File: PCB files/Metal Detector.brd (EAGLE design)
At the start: 100 x 80 mm, 61 parts, among them IC1 NE5534AD, IC2 BQ24133RGYR, IC3 MC33269D-5.0G, IC4 ESP32-WROOM-32UE-N4, IC5 CP2102, IC6 NCP1117DT12G, Q1 IRF740, Q2 BC556, Q4 MBT3904DW1T1, T1 BC547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

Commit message: Add files via upload
Design process still on progress
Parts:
- added C6: 1uF/16v, rcl:C0603
- added R13: 10R, rcl:R1206
- added R15: 2R2, rcl:R2010
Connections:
- removed net 1: X2.1
- removed net 2: X2.2
- removed net 3: X2.3
- new net EXT_PWR_IN: IC3.4, IC6.3, X2.2
- new net N$14: C6.2, IC2.4, R13.2
- net GND: now also IC3.1, IC6.1, X2.1, X2.3
- net VCC: now also IC6.2
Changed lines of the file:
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@@
 <attribute name="VALUE" x="-114.34" y="-165.1" size="1.27" layer="27" align="center"/>
+</element>
+<element name="C6" library="rcl" library_urn="urn:adsk.eagle:library:334" package="C0603" package3d_urn="urn:adsk.eagle:package:23616/2" value="1uF/16v" x="-120.65" y="-175.26" smashed="yes">
+<attribute name="NAME" x="-121.285" y="-174.625" size="1.27" layer="25"/>
+<attribute name="POPULARITY" value="73" x="-120.65" y="-175.26" size="1.778" layer="27" display="off"/>
+<attribute name="SPICEPREFIX" value="C" x="-120.65" y="-175.26" size="1.778" layer="27" display="off"/>
+<attribute name="VALUE" x="-121.285" y="-177.165" size="1.27" layer="27"/>
+</element>
+<element name="R15" library="rcl" library_urn="urn:adsk.eagle:library:334" package="R2010" package3d_urn="urn:adsk.eagle:package:23551/2" value="2R2" x="-119.38" y="-232.41" smashed="yes">
+<attribute name="NAME" x="-122.555" y="-230.505" size="1.27" layer="25"/>
+<attribute name="POPULARITY" value="3" x="-119.38" y="-232.41" size="1.778" layer="27" display="off"/>
+<attribute name="SPICEPREFIX" value="R" x="-119.38" y="-232.41" size="1.778" layer="27" display="off"/>
+<attribute name="VALUE" x="-122.555" y="-235.585" size="1.27" layer="27"/>
+</element>
+<element name="R13" library="rcl" library_urn="urn:adsk.eagle:library:334" package="R1206" package3d_urn="urn:adsk.eagle:package:23540/2" value="10R" x="-120.65" y="-240.03" smashed="yes">
+<attribute name="NAME" x="-121.92" y="-238.76" size="1.27" layer="25"/>
+<attribute name="POPULARITY" value="41" x="-120.65" y="-240.03" size="1.778" layer="27" display="off"/>
+<attribute name="SPICEPREFIX" value="R" x="-120.65" y="-240.03" size="1.778" layer="27" display="off"/>
+<attribute name="VALUE" x="-121.92" y="-242.57" size="1.27" layer="27"/>
 </element>
 </elements>
@@
 <contactref element="D4" pad="2"/>
 <contactref element="D8" pad="2"/>
+<contactref element="X2" pad="1"/>
+<contactref element="X2" pad="3"/>
+<contactref element="IC6" pad="1"/>
+<contactref element="IC3" pad="1"/>
+<wire x1="-75.102" y1="-86.995" x2="-67.25" y2="-98.805" width="0" layer="19" extent="1-1"/>
+<wire x1="-73.66" y1="-79.5528" x2="-75.102" y2="-86.995" width="0" layer="19" extent="1-1"/>
+<wire x1="-68.6562" y1="-76.5556" x2="-73.66" y2="-79.5528" width="0" layer="19" extent="1-1"/>
+<wire x1="-68.255" y1="-59.69" x2="-68.6562" y2="-76.5556" width="0" layer="19" extent="1-1"/>
+<wire x1="-74.51" y1="-50.8" x2="-68.255" y2="-59.69" width="0" layer="19" extent="1-1"/>
 <wire x1="-72.81" y1="-45.72" x2="-74.51" y2="-50.8" width="0" layer="19" extent="1-1"/>
 <wire x1="-74.51" y1="-40.64" x2="-72.81" y2="-45.72" width="0" layer="19" extent="1-1"/>
@@
 <wire x1="-72.25" y1="-13.18" x2="-66.4" y2="-19.12" width="0" layer="19" extent="1-1"/>
 <wire x1="-54.75" y1="-13.18" x2="-63.6" y2="-19.12" width="0" layer="19" extent="1-1"/>
-<wire x1="-68.255" y1="-59.69" x2="-74.51" y2="-50.8" width="0" layer="19" extent="1-1"/>
 <wire x1="-44.265" y1="-19.08" x2="-54.75" y2="-13.18" width="0" layer="19" extent="1-1"/>
 <wire x1="-41.72" y1="-13.47" x2="-44.265" y2="-19.08" width="0" layer="19" extent="1-1"/>
@@
 <contactref element="R18" pad="2"/>
 <contactref element="F2" pad="2"/>
+<contactref element="IC6" pad="2"/>
+<wire x1="-64.64" y1="-55.88" x2="-74.43" y2="-96.52" width="0" layer="19" extent="1-1"/>
 <wire x1="-63.92" y1="-50.8" x2="-64.64" y2="-55.88" width="0" layer="19" extent="1-1"/>
 <wire x1="-58.84" y1="-50.8" x2="-63.92" y2="-50.8" width="0" layer="19" extent="1-1"/>
@@
 <wire x1="-39.87" y1="-11.62" x2="-40.22" y2="-50.8" width="0" layer="19" extent="1-1"/>
 </signal>
-<signal name="1">
-<contactref element="X2" pad="1"/>
-</signal>
-<signal name="2">
+<signal name="EXT_PWR_IN">
 <contactref element="X2" pad="2"/>
-</signal>
-<signal name="3">
-<contactref element="X2" pad="3"/>
+<contactref element="IC3" pad="4"/>
+<contactref element="IC6" pad="3"/>
+<wire x1="-67.25" y1="-94.235" x2="-75.102" y2="-90.805" width="0" layer="19" extent="1-1"/>
+<wire x1="-68.6562" y1="-82.55" x2="-75.102" y2="-90.805" width="0" layer="19" extent="1-1"/>
+</signal>
+<signal name="N$14">
+<contactref element="IC2" pad="4"/>
+<contactref element="C6" pad="2"/>
+<contactref element="R13" pad="2"/>
+<wire x1="-119.8" y1="-175.26" x2="-71.1" y2="-66.495" width="0" layer="19" extent="1-1"/>
+<wire x1="-119.228" y1="-240.03" x2="-119.8" y2="-175.26" width="0" layer="19" extent="1-1"/>
 </signal>
 </signals>

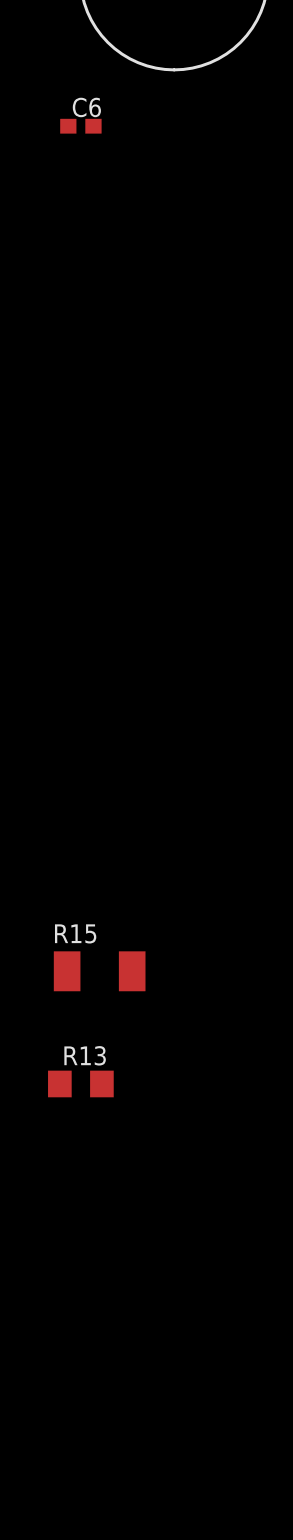
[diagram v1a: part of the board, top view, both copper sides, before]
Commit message: Add files via upload
Still designin power circuit but should be change battery charge IC for tehnical limitation
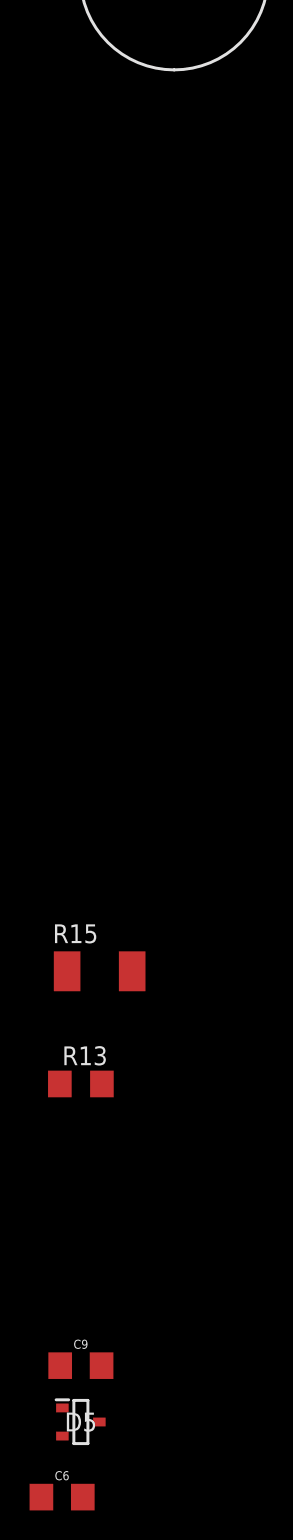
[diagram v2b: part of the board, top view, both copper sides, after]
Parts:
- added C9: 1.0uF/25 VDC/XR7, SparkFun-Capacitors:1206
- added D5: MMBD717, MMBD717:SOT95P240X110-3N
- C6: value 1uF/16v -> 2.2uF/25 VDC/XR7; device rcl:C0603 -> SparkFun-Capacitors:1206
- moved C6 92.7 mm to (-121.9, -268.0)
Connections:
- new net ACDRV: IC2.8
- new net ACN: IC2.5
- new net ACP: IC2.6
- new net ACSET: IC2.17
- new net AGND: IC2.25
- new net AVCC: C9.1, IC2.4, R13.2
- new net BATDRV: IC2.19
- new net BTST: IC2.21
- new net CELL: IC2.14
- new net CMSRC: IC2.7
- new net ISET: IC2.13
- new net N$16: C6.1, R15.1
- new net OVPSET: IC2.18
- new net PGND_1: IC2.22
- new net PGND_2: IC2.23
- new net PVCC_1: IC2.2
- new net PVCC_2: IC2.3
- new net REGN: IC2.20
- new net SRN: IC2.15
- new net SRP: IC2.16
- new net STAT: IC2.9
- new net SW_1: IC2.1
- new net SW_2: IC2.24
- new net TS: IC2.10
- new net TTC: IC2.11
- new net VBATT: D5.K2
- new net VREF: IC2.12
- net EXT_PWR_IN: now also D5.K1, R15.2
- net GND: now also C6.2, C9.2
- net N$14: now also D5.A, R13.1; no longer C6.2, IC2.4, R13.2
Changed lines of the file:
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@@
 <attribute name="VALUE" x="-114.34" y="-165.1" size="1.27" layer="27" align="center"/>
-</element>
-<element name="C6" library="rcl" library_urn="urn:adsk.eagle:library:334" package="C0603" package3d_urn="urn:adsk.eagle:package:23616/2" value="1uF/16v" x="-120.65" y="-175.26" smashed="yes">
-<attribute name="NAME" x="-121.285" y="-174.625" size="1.27" layer="25"/>
-<attribute name="POPULARITY" value="73" x="-120.65" y="-175.26" size="1.778" layer="27" display="off"/>
-<attribute name="SPICEPREFIX" value="C" x="-120.65" y="-175.26" size="1.778" layer="27" display="off"/>
-<attribute name="VALUE" x="-121.285" y="-177.165" size="1.27" layer="27"/>
 </element>
 <element name="R15" library="rcl" library_urn="urn:adsk.eagle:library:334" package="R2010" package3d_urn="urn:adsk.eagle:package:23551/2" value="2R2" x="-119.38" y="-232.41" smashed="yes">
@@
 <attribute name="SPICEPREFIX" value="R" x="-120.65" y="-240.03" size="1.778" layer="27" display="off"/>
 <attribute name="VALUE" x="-121.92" y="-242.57" size="1.27" layer="27"/>
+</element>
+<element name="C9" library="SparkFun-Capacitors" library_urn="urn:adsk.eagle:library:510" package="1206" package3d_urn="urn:adsk.eagle:package:41385095/1" value="1.0uF/25 VDC/XR7" x="-120.65" y="-259.08" smashed="yes">
+<attribute name="NAME" x="-120.65" y="-257.937" size="0.6096" layer="25" font="vector" ratio="20" align="bottom-center"/>
+<attribute name="PROD_ID" value="CAP-09822" x="-120.65" y="-259.08" size="1.778" layer="27" display="off"/>
+<attribute name="VALUE" x="-120.65" y="-260.223" size="0.6096" layer="27" font="vector" ratio="20" align="top-center"/>
+</element>
+<element name="D5" library="MMBD717" package="SOT95P240X110-3N" value="MMBD717" x="-120.65" y="-262.89" smashed="yes">
+<attribute name="ARROW_PART_NUMBER" value="" x="-120.65" y="-262.89" size="1.778" layer="27" display="off"/>
+<attribute name="ARROW_PRICE-STOCK" value="" x="-120.65" y="-262.89" size="1.778" layer="27" display="off"/>
+<attribute name="DESCRIPTION" value="Small Signal Schottky (IF&lt;1A) - MMBD717 , 20V, 1mA, SOT-23" x="-120.65" y="-262.89" size="1.778" layer="27" display="off"/>
+<attribute name="HEIGHT" value="1.1mm" x="-120.65" y="-262.89" size="1.778" layer="27" display="off"/>
+<attribute name="MANUFACTURER_NAME" value="PANJIT" x="-120.65" y="-262.89" size="1.778" layer="27" display="off"/>
+<attribute name="MANUFACTURER_PART_NUMBER" value="MMBD717" x="-120.65" y="-262.89" size="1.778" layer="27" display="off"/>
+<attribute name="MOUSER_PART_NUMBER" value="" x="-120.65" y="-262.89" size="1.778" layer="27" display="off"/>
+<attribute name="MOUSER_PRICE-STOCK" value="" x="-120.65" y="-262.89" size="1.778" layer="27" display="off"/>
+<attribute name="NAME" x="-120.65" y="-262.89" size="1.27" layer="25" align="center"/>
+<attribute name="VALUE" x="-120.65" y="-262.89" size="1.27" layer="27" align="center"/>
+</element>
+<element name="C6" library="SparkFun-Capacitors" library_urn="urn:adsk.eagle:library:510" package="1206" package3d_urn="urn:adsk.eagle:package:41385095/1" value="2.2uF/25 VDC/XR7" x="-121.92" y="-267.97" smashed="yes">
+<attribute name="NAME" x="-121.92" y="-266.827" size="0.6096" layer="25" font="vector" ratio="20" align="bottom-center"/>
+<attribute name="PROD_ID" value="CAP-09822" x="-121.92" y="-267.97" size="1.778" layer="27" display="off"/>
+<attribute name="VALUE" x="-121.92" y="-269.113" size="0.6096" layer="27" font="vector" ratio="20" align="top-center"/>
 </element>
 </elements>
@@
 <contactref element="IC6" pad="1"/>
 <contactref element="IC3" pad="1"/>
+<contactref element="C9" pad="2"/>
+<contactref element="C6" pad="2"/>
 <wire x1="-75.102" y1="-86.995" x2="-67.25" y2="-98.805" width="0" layer="19" extent="1-1"/>
 <wire x1="-73.66" y1="-79.5528" x2="-75.102" y2="-86.995" width="0" layer="19" extent="1-1"/>
@@
 <wire x1="-31.17" y1="77.47" x2="-34.98" y2="77.47" width="0" layer="19" extent="1-1"/>
 <wire x1="-26.67" y1="66.04" x2="-31.17" y2="77.47" width="0" layer="19" extent="1-1"/>
+<wire x1="-119.25" y1="-259.08" x2="-67.25" y2="-98.805" width="0" layer="19" extent="1-1"/>
+<wire x1="-120.52" y1="-267.97" x2="-119.25" y2="-259.08" width="0" layer="19" extent="1-1"/>
 </signal>
 <signal name="VCC">
@@
 <contactref element="IC3" pad="4"/>
 <contactref element="IC6" pad="3"/>
+<contactref element="R15" pad="2"/>
+<contactref element="D5" pad="K1"/>
 <wire x1="-67.25" y1="-94.235" x2="-75.102" y2="-90.805" width="0" layer="19" extent="1-1"/>
 <wire x1="-68.6562" y1="-82.55" x2="-75.102" y2="-90.805" width="0" layer="19" extent="1-1"/>
+<wire x1="-117.18" y1="-232.41" x2="-67.25" y2="-94.235" width="0" layer="19" extent="1-1"/>
+<wire x1="-121.9" y1="-261.94" x2="-117.18" y2="-232.41" width="0" layer="19" extent="1-1"/>
+</signal>
+<signal name="N$16">
+<contactref element="C6" pad="1"/>
+<contactref element="R15" pad="1"/>
+<wire x1="-121.58" y1="-232.41" x2="-123.32" y2="-267.97" width="0" layer="19" extent="1-1"/>
+</signal>
+<signal name="AVCC">
+<contactref element="IC2" pad="4"/>
+<contactref element="R13" pad="2"/>
+<contactref element="C9" pad="1"/>
+<wire x1="-119.228" y1="-240.03" x2="-71.1" y2="-66.495" width="0" layer="19" extent="1-1"/>
+<wire x1="-122.05" y1="-259.08" x2="-119.228" y2="-240.03" width="0" layer="19" extent="1-1"/>
+</signal>
+<signal name="VBATT">
+<contactref element="D5" pad="K2"/>
 </signal>
 <signal name="N$14">
-<contactref element="IC2" pad="4"/>
-<contactref element="C6" pad="2"/>
-<contactref element="R13" pad="2"/>
-<wire x1="-119.8" y1="-175.26" x2="-71.1" y2="-66.495" width="0" layer="19" extent="1-1"/>
-<wire x1="-119.228" y1="-240.03" x2="-119.8" y2="-175.26" width="0" layer="19" extent="1-1"/>
+<contactref element="D5" pad="A"/>
+<contactref element="R13" pad="1"/>
+<wire x1="-122.072" y1="-240.03" x2="-119.4" y2="-262.89" width="0" layer="19" extent="1-1"/>
+</signal>
+<signal name="PVCC_1">
+<contactref element="IC2" pad="2"/>
+</signal>
+<signal name="PVCC_2">
+<contactref element="IC2" pad="3"/>
+</signal>
+<signal name="ACN">
+<contactref element="IC2" pad="5"/>
+</signal>
+<signal name="ACP">
+<contactref element="IC2" pad="6"/>
+</signal>
+<signal name="CMSRC">
+<contactref element="IC2" pad="7"/>
+</signal>
+<signal name="ACDRV">
+<contactref element="IC2" pad="8"/>
+</signal>
+<signal name="STAT">
+<contactref element="IC2" pad="9"/>
+</signal>
+<signal name="TS">
+<contactref element="IC2" pad="10"/>
+</signal>
+<signal name="TTC">
+<contactref element="IC2" pad="11"/>
+</signal>
+<signal name="VREF">
+<contactref element="IC2" pad="12"/>
+</signal>
+<signal name="ISET">
+<contactref element="IC2" pad="13"/>
+</signal>
+<signal name="CELL">
+<contactref element="IC2" pad="14"/>
+</signal>
+<signal name="SRN">
+<contactref element="IC2" pad="15"/>
+</signal>
+<signal name="SRP">
+<contactref element="IC2" pad="16"/>
+</signal>
+<signal name="ACSET">
+<contactref element="IC2" pad="17"/>
+</signal>
+<signal name="OVPSET">
+<contactref element="IC2" pad="18"/>
+</signal>
+<signal name="BATDRV">
+<contactref element="IC2" pad="19"/>
+</signal>
+<signal name="REGN">
+<contactref element="IC2" pad="20"/>
+</signal>
+<signal name="BTST">
+<contactref element="IC2" pad="21"/>
+</signal>
+<signal name="PGND_1">
+<contactref element="IC2" pad="22"/>
+</signal>
+<signal name="PGND_2">
+<contactref element="IC2" pad="23"/>
+</signal>
+<signal name="AGND">
+<contactref element="IC2" pad="25"/>
+</signal>
+<signal name="SW_1">
+<contactref element="IC2" pad="1"/>
+</signal>
+<signal name="SW_2">
+<contactref element="IC2" pad="24"/>
 </signal>
 </signals>

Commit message: Add files via upload
Adding Voltage Regulator Circuits
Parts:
- added C10, C13: 1uF, resistor:085CS_1AR
- added C11, C14: 10uF, resistor:085CS_1AR
- added C12, C8: 0.1uF, rcl:C075-052X106
- added D10, D11, D6, D7: 1N4002, diode:DO41-10
- added J1: L-KLS1-TSJ3.5-013, L-KLS1-TSJ3.5-013:LKLS1TSJ35013
- added R14, R24: 240Ω, rcl:R0805
- added R16: 394Ω, rcl:R0805
- added R25: 720Ω, rcl:R0805
- IC3: value MC33269D-5.0G -> LM317MBSTT3; device MC33269D-5.0G:SOIC127P600X175-8N -> v-reg:SOT223
- IC6: value NCP1117DT12G -> LM317MBSTT3; device NCP1117DT12G:NVD5117PLT4GVF01 -> v-reg:SOT223
- R1, R17, R18, R20, R21, R22: value 10K -> 10KΩ
- R10, TR1: value 1K -> 1KΩ
- R13: value 10R -> 10RΩ
- R15: value 2R2 -> 2R2Ω
- R19: value 4K7 -> 4K7Ω
- R2: value 1R -> 1RΩ
- R3: value 2k2 -> 2k2Ω
- R4: value 4k7 -> 4k7Ω
- R6: value 100k -> 100kΩ
- R7: value 10k -> 10kΩ
- R8: value 22K -> 22KΩ
- R9: value 1M -> 1MΩ
- moved IC6 233.1 mm to (-121.9, -325.1)
- moved IC3 200.5 mm to (-121.9, -283.2)
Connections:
- new net N$15: C11.+, D7.A, IC3.1, R24.1, R25.2
- new net N$20: C14.+, D11.A, IC6.1, R14.1, R16.2
- net EXT_PWR_IN: now also C12.1, C8.1, D10.C, D6.C, IC3.3; no longer D5.K1, IC3.4, R15.2
- net GND: now also C10.-, C11.-, C12.2, C13.-, C14.-, C8.2, R16.1, R25.1; no longer IC3.1, IC6.1
- net VCC: now also C10.+, C13.+, D10.A, D11.C, D6.A, D7.C, IC3.4, IC6.4, R14.2, R24.2; no longer IC6.2

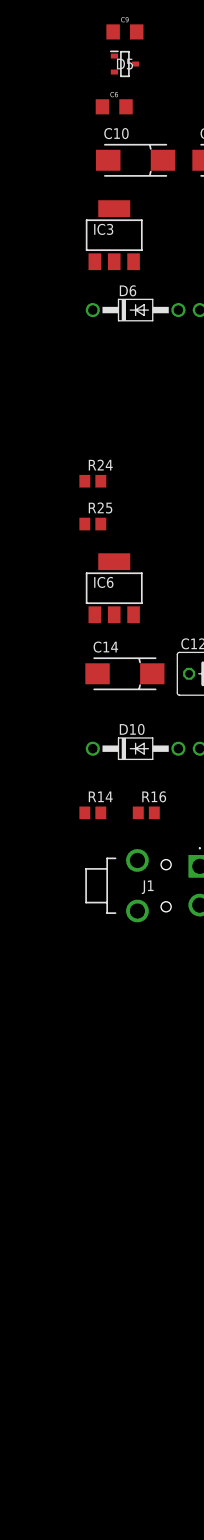
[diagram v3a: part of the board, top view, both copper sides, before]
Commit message: Add files via upload
Still designing battery charger and power line managment circuit
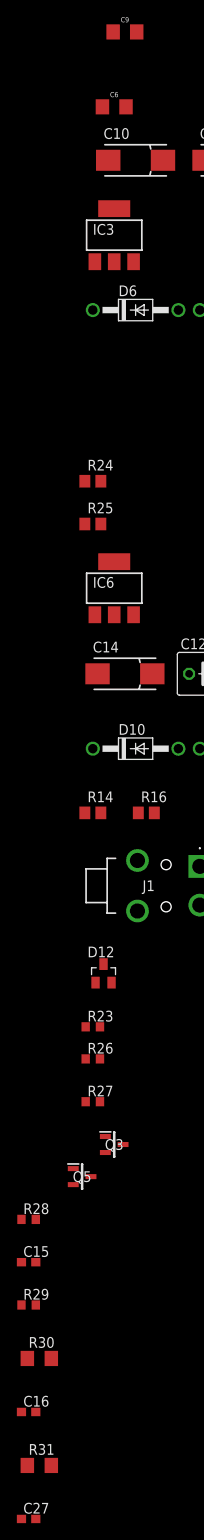
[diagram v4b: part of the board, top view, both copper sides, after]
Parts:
- removed D5: MMBD717, MMBD717:SOT95P240X110-3N
- added C15: 0.047uF, rcl:C0603
- added C16, C27: 0.1uF, rcl:C0603
- added D12: BAT54C, diode:SOT23
- added Q3, Q5: SI2312CDS-T1-GE3, SI2312CDS-T1-GE3:SOT95P237X112-3N
- added R23: 1000kΩ, rcl:R0603
- added R26: 100kΩ, rcl:R0603
- added R27, R28: 4.02kΩ, rcl:R0603
- added R29: 499kΩ, rcl:R0603
- added R30: 0.02RΩ, rcl:R1206
- added R31: 0RΩ, rcl:R1206
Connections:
- new net N$21: C15.1, Q3.2, Q5.3, R27.2, R29.2
- new net N$22: C15.2, Q3.1, Q5.1, R28.2, R29.1
- new net N$24: R30.2, R31.2
- net ACDRV: now also R28.1
- net ACN: now also C16.1, R31.1
- net ACP: now also C16.2, C27.2, Q5.2, R30.1
- net CMSRC: now also R27.1
- net EXT_PWR_IN: now also D12.1, Q3.3, R15.2, R23.2
- net GND: now also C27.1, R26.1
- net N$14: now also D12.3; no longer D5.A
- net OVPSET: now also R23.1, R26.2
- net VBATT: now also D12.2; no longer D5.K2
